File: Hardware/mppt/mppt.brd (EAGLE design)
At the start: 84.8 x 80 mm, 37 parts, among them M1 IRLZ34N, M2 IRLZ34N, M3 IRLZ34N

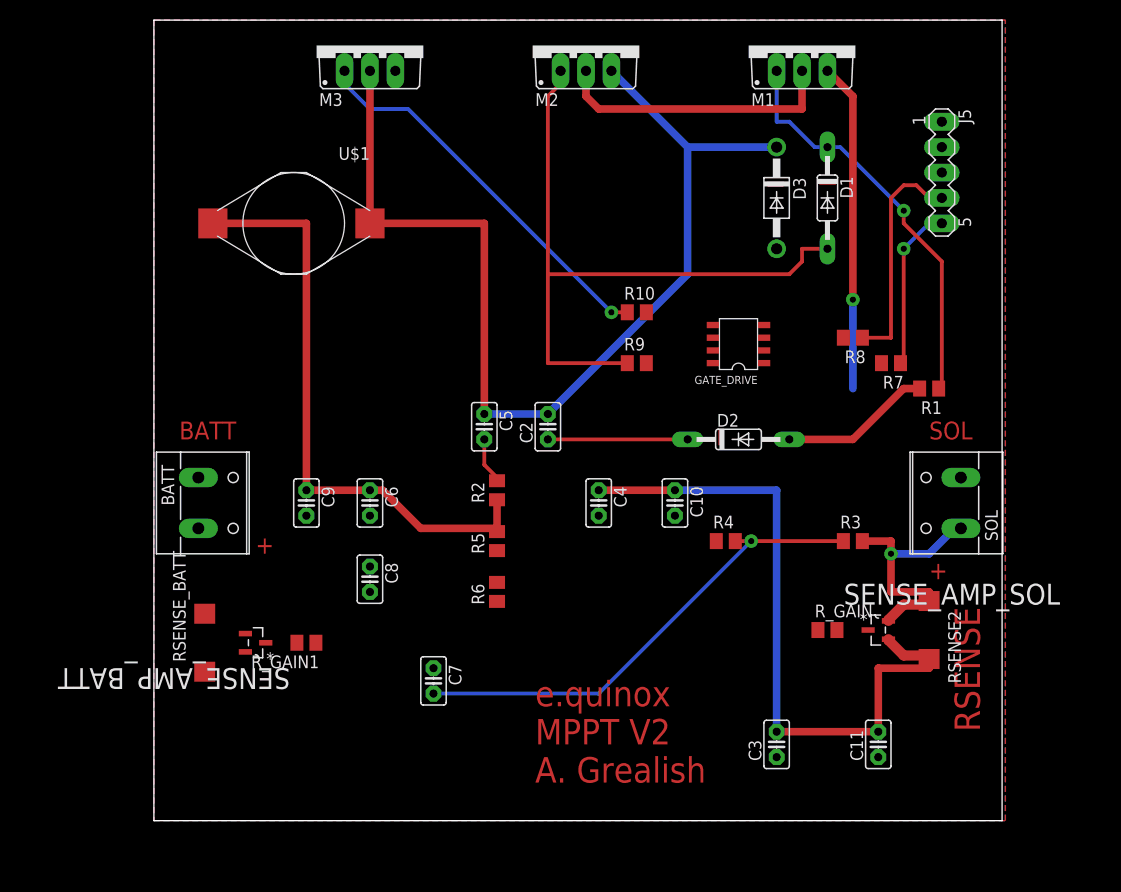
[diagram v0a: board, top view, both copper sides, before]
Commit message: Added lates MPPT Tracking PCB design
Also cleaned hardware folder, removing non-working current sense
designs.
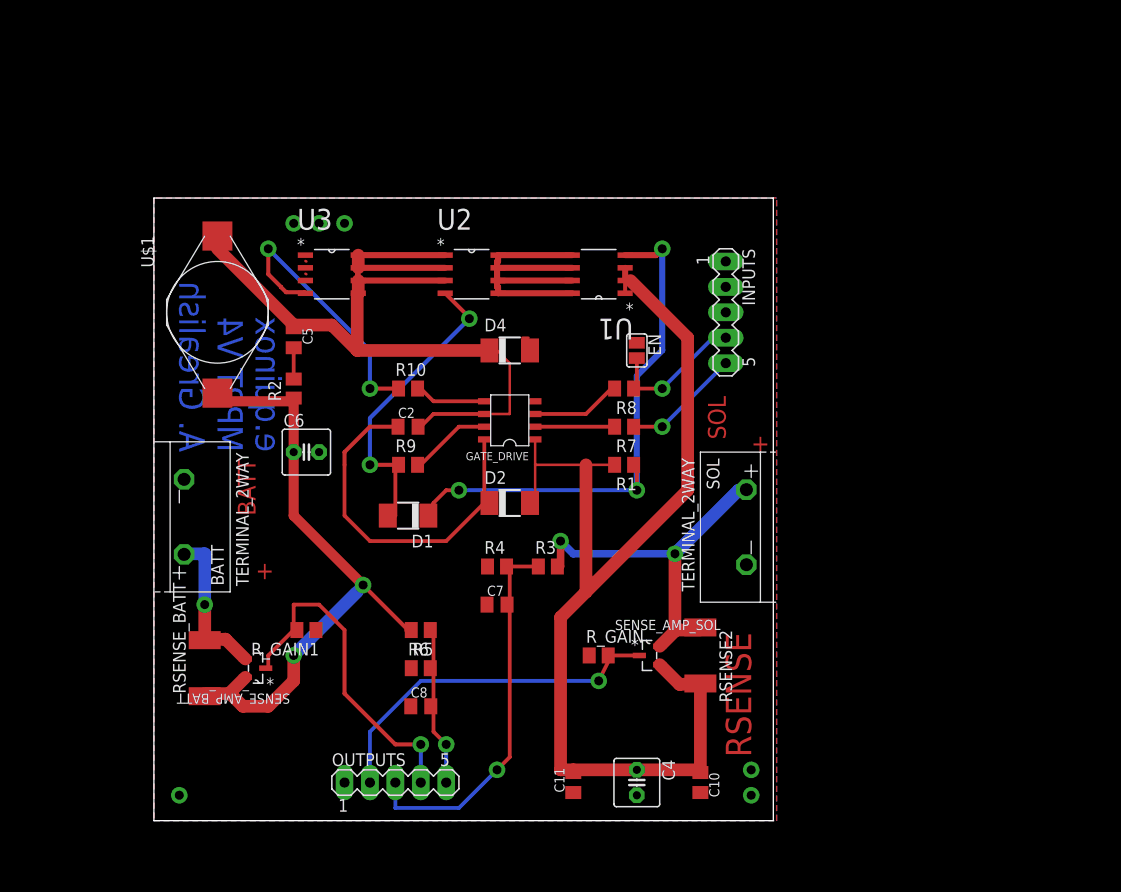
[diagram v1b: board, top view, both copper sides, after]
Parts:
- removed C3: 100uF, capacitor-wima:C2.5-2
- removed C9: 1uF, capacitor-wima:C2.5-2
- removed D3: UF4007, diode:DO41-10
- removed J5: (no value), con-lstb:MA05-1
- removed M1, M2, M3: IRLZ34N, transistor-power:TO220BV
- added D4: US1D - 1625280, diode:DO-214AC
- added EN: (no value), jumper:SJ
- added INPUTS, OUTPUTS: (no value), con-lstb:MA05-1
- added U1, U2, U3: DMS3016SSS-13, equinox:SOIC127P600X175-8N
- BATT, SOL: value (none) -> TERMINAL_2WAY; device con-wago-508:W237-132 -> equinox:TERMINAL_2WAY
- C10, C11, C2, C5: device capacitor-wima:C2.5-2 -> resistor:C0805K
- C4: device capacitor-wima:C2.5-2 -> resistor:C025-050X050
- C6: value 100uF -> 220uF; device capacitor-wima:C2.5-2 -> resistor:C025-050X050
- C7, C8: value 1uF -> 0.1uF; device capacitor-wima:C2.5-2 -> resistor:C0805K
- D1, D2: value 1N4001 -> S1A-E3/5AT; device diode:DO35-10 -> diode:DO-214AC
- RSENSE2, RSENSE_BATT: device rcl:R2512W -> rcl:R2512
- moved D1 52.6 mm to (25.4, 30.5), turned to 180 degrees
- moved R1 31.4 mm to (47.0, 35.6)
- moved C11 30.7 mm to (41.9, 3.81)
- moved R3 30.6 mm to (39.4, 25.4)
- moved C4 28.2 mm to (48.3, 3.81)
- moved C10 28.1 mm to (54.6, 3.81)
- moved R7 27.4 mm to (47.0, 39.4)
- moved SOL 25.9 mm to (54.6, 36.8), turned to 270 degrees
- moved R9 25.0 mm to (25.4, 35.6)
- moved GATE_DRIVE 24.1 mm to (38.1, 41.9)
- moved R10 24.1 mm to (25.4, 43.2)
- moved D2 23.7 mm to (35.6, 31.8)
- moved R8 23.4 mm to (47.0, 43.2)
- moved R4 23.0 mm to (34.3, 25.4)
- moved RSENSE2 23.0 mm to (54.6, 16.5)
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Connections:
- removed net BATT_AMPS: R_GAIN1.2, SENSE_AMP_BATT.1
- removed net BAT_VOLTS: C8.2, R5.1, R6.2
- removed net SOL_AMPS: R_GAIN.2, SENSE_AMP_SOL.1
- removed net SOL_VOLTS: C7.2, R3.1, R4.2
- new net BATT_I: OUTPUTS.4, R_GAIN1.2, SENSE_AMP_BATT.1
- new net BATT_V: C8.2, OUTPUTS.5, R5.1, R6.2
- new net SOL_I: OUTPUTS.2, R_GAIN.2, SENSE_AMP_SOL.1
- new net SOL_V: C7.2, OUTPUTS.3, R3.1, R4.2
- net EN_: now also EN.2, INPUTS.4; no longer J5.4
- net GND: now also BATT.P$2, D4.A, EN.1, INPUTS.1, INPUTS.2, INPUTS.3, OUTPUTS.1, SOL.P$2, U3.1, U3.2, U3.3; no longer BATT.1, C3.1, C9.2, D3.A, M3.S, SOL.2
- net N$11: now also R10.1, U3.4; no longer C2.2, C5.1, D3.C, GATE_DRIVE.6, M2.S, M3.D, U$1.P$1
- net N$12: no longer C9.1
- net N$14: now also U2.4; no longer M2.G
- net N$16: now also SOL.P$1; no longer SOL.1
- net N$3: now also BATT.P$1; no longer BATT.2
- net N$4: now also C2.2, C5.1, D4.C, GATE_DRIVE.6, U$1.P$1, U2.1, U2.2, U2.3, U3.5, U3.6, U3.7, U3.8; no longer M3.G, R10.1
- net N$5: now also U1.4; no longer M1.G
- net N$6: now also U1.5, U1.6, U1.7, U1.8, U2.5, U2.6, U2.7, U2.8; no longer M1.D, M2.D
- net N$9: now also U1.1, U1.2, U1.3; no longer C3.2, M1.S
- net PWM: now also INPUTS.5; no longer J5.5
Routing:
- net N$11: track 104.2 -> 28.1 mm, vias 0 -> 2
- net SOL_VOLTS: track 48.9 -> 0.00 mm, vias 1 -> 0
- net N$4: track 39.0 -> 87.4 mm, vias 1 -> 0
- net SOL_V: track 0.00 -> 38.6 mm, vias 0 -> 1
- net N$14: track 67.4 -> 31.3 mm, vias 0 -> 2
- net SOL_I: track 0.00 -> 36.0 mm, vias 0 -> 1
- net BATT_I: track 0.00 -> 34.0 mm, vias 0 -> 1
- net N$10: track 14.0 -> 36.2 mm
- net BATT_V: track 0.00 -> 16.7 mm, vias 0 -> 1
- net N$3: track 0.00 -> 15.6 mm, vias 0 -> 1
- net N$5: track 41.1 -> 54.2 mm, vias 1 -> 3
- net N$16: track 25.6 -> 37.3 mm, vias 1 -> 2
- net N$2: track 0.00 -> 8.99 mm
- net EN_: track 23.0 -> 14.4 mm, vias 0 -> 1
- net N$7: track 0.00 -> 8.25 mm
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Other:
- board size 84.8 x 80 mm -> 61.9 x 62.2 mm
- board text added: "A. Grealish"
- board text added: "MPPT V4"
- board text added: "e.quinox"
- board text removed: "-"
- board text removed: "e.quinox MPPT V2 A. Grealish"

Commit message: Some updates to MPPT hardware and software
The design now can charge lead acid batteries but no high/low voltage
cut-out is enabled.
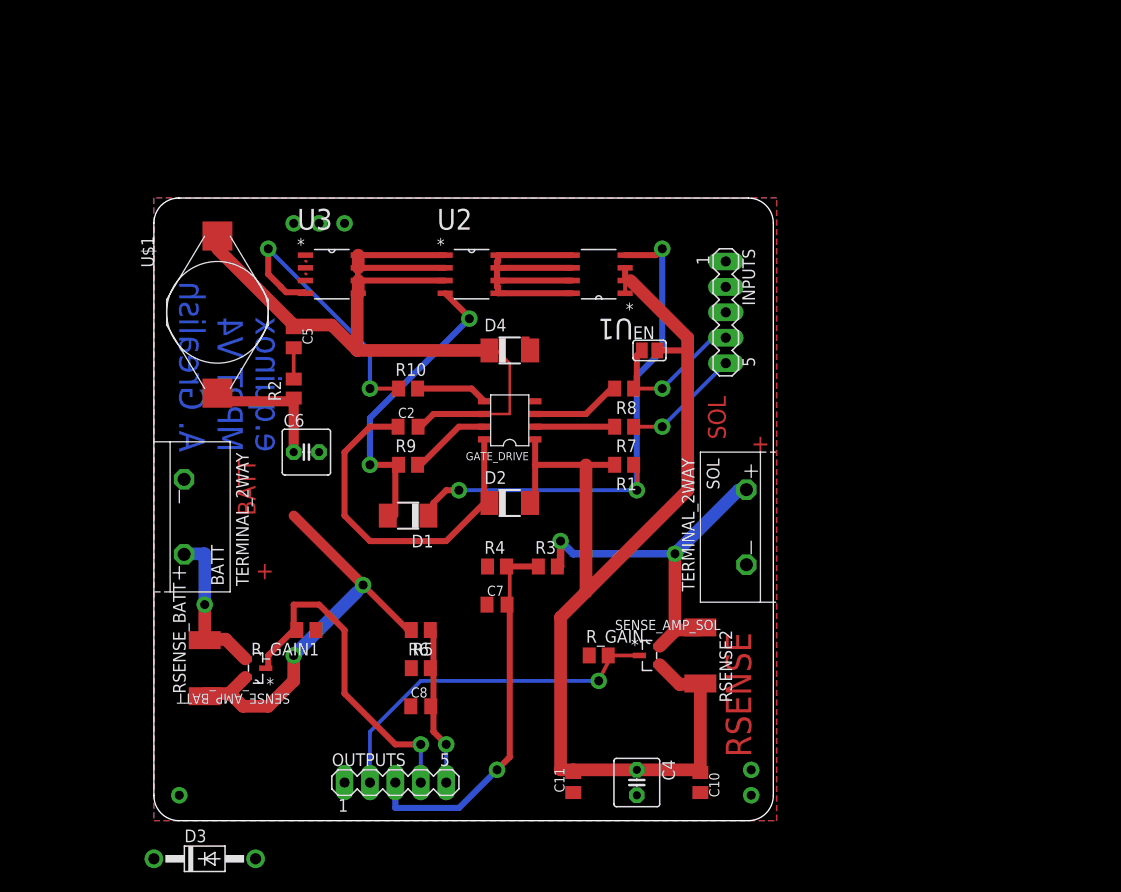
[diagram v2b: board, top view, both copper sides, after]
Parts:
- added D3: 1N4004, diode:DO41-10
- U$1: value (none) -> 330uF
- moved EN 1.27 mm to (49.5, 47.0), turned to 0 degrees
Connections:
- new net N$1: C6.1, D3.A, R2.1, U$1.P$2
- net EN_: now also EN.1; no longer EN.2
- net GND: no longer EN.1
- net N$12: now also D3.C; no longer C6.1, R2.1, U$1.P$2
- net N$9: now also EN.2
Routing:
- net N$12: track 62.1 -> 41.9 mm
- net N$1: track 0.00 -> 13.8 mm
- net N$9: track 115.1 -> 118.2 mm
- net EN_: track 14.4 -> 15.3 mm
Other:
- outline, holes or cut-outs redrawn
